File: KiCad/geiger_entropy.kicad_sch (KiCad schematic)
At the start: 34 parts, among them J1 AudioJack2, J2 Jack-DC, J3 ICSP, J4 Conn_01x04_Socket, J5 Conn_01x10_Pin, J6 Conn_01x10_Pin, SW1 RESET, SW2 REV, SW3 FWD, U1 LM393, U2 L7805, U4 ATmega328-P, Y1 16MHz

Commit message: Add BOM and fix signal line debounce issue with a 100pF capacitor - optimise PCB layout
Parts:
- added C11: 100pF, Capacitor_THT:C_Disc_D5.0mm_W2.5mm_P5.00mm, symbol Device:C
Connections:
- net D2: now also C11.1
- net GND: now also C11.2
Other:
- moved on the sheet: L1, R7
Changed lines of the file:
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@@
 	)
 	(junction
+		(at 171.45 105.41)
+		(diameter 0)
+		(color 0 0 0 0)
+	)
+	(junction
 		(at 76.2 91.44)
 		(diameter 0)
@@
 	(wire
 		(pts
+			(xy 171.45 110.49) (xy 171.45 105.41)
+		)
+		(stroke
+			(width 0)
+			(type default)
+		)
+	)
+	(wire
+		(pts
 			(xy 236.22 142.24) (xy 247.65 142.24)
 		)
@@
 	(wire
 		(pts
-			(xy 151.13 69.85) (xy 165.1 69.85)
+			(xy 151.13 69.85) (xy 171.45 69.85)
 		)
 		(stroke
@@
 	(wire
 		(pts
+			(xy 171.45 105.41) (xy 177.8 105.41)
+		)
+		(stroke
+			(width 0)
+			(type default)
+		)
+	)
+	(wire
+		(pts
 			(xy 215.9 31.75) (xy 222.25 31.75)
 		)
@@
 	(wire
 		(pts
+			(xy 171.45 125.73) (xy 171.45 118.11)
+		)
+		(stroke
+			(width 0)
+			(type default)
+		)
+	)
+	(wire
+		(pts
 			(xy 68.58 153.67) (xy 74.93 153.67)
 		)
@@
 	(wire
 		(pts
-			(xy 151.13 105.41) (xy 157.48 105.41)
+			(xy 151.13 105.41) (xy 171.45 105.41)
 		)
 		(stroke
@@
 	)
 	(label "Signal"
-		(at 157.48 105.41 0)
+		(at 177.8 105.41 0)
 		(effects
 			(font
@@
 	(symbol
 		(lib_id "Device:LED")
-		(at 165.1 81.28 90)
+		(at 171.45 81.28 90)
 		(unit 1)
 		(body_style 1)
@@
 		(fields_autoplaced yes)
 		(property "Reference" "L1"
-			(at 168.91 81.5974 90)
+			(at 175.26 81.5974 90)
 			(show_name no)
 			(do_not_autoplace no)
@@
 		)
 		(property "Value" "Yellow"
-			(at 168.91 84.1374 90)
+			(at 175.26 84.1374 90)
 			(show_name no)
 			(do_not_autoplace no)
@@
 		)
 		(property "Footprint" "LED_THT:LED_D3.0mm"
-			(at 165.1 81.28 0)
+			(at 171.45 81.28 0)
 			(hide yes)
 			(show_name no)
@@
 		)
 		(property "Datasheet" ""
-			(at 165.1 81.28 0)
+			(at 171.45 81.28 0)
 			(hide yes)
 			(show_name no)
@@
 		)
 		(property "Description" "Light emitting diode"
-			(at 165.1 81.28 0)
+			(at 171.45 81.28 0)
 			(hide yes)
 			(show_name no)
@@
 		)
 		(property "Sim.Pins" "1=K 2=A"
-			(at 165.1 81.28 0)
+			(at 171.45 81.28 0)
 			(hide yes)
 			(show_name no)
@@
 	)
 	(symbol
+		(lib_id "power:GND")
+		(at 171.45 125.73 0)
+		(unit 1)
+		(body_style 1)
+		(exclude_from_sim no)
+		(in_bom yes)
+		(on_board yes)
+		(in_pos_files yes)
+		(dnp no)
+		(fields_autoplaced yes)
+		(property "Reference" "#PWR019"
+			(at 171.45 132.08 0)
+			(hide yes)
+			(show_name no)
+			(do_not_autoplace no)
+			(effects
+				(font
+					(size 1.27 1.27)
+				)
+			)
+		)
+		(property "Value" "GND"
+			(at 171.45 130.81 0)
+			(show_name no)
+			(do_not_autoplace no)
+			(effects
+				(font
+					(size 1.27 1.27)
+				)
+			)
+		)
+		(property "Footprint" ""
+			(at 171.45 125.73 0)
+			(hide yes)
+			(show_name no)
+			(do_not_autoplace no)
+			(effects
+				(font
+					(size 1.27 1.27)
+				)
+			)
+		)
+		(property "Datasheet" ""
+			(at 171.45 125.73 0)
+			(hide yes)
+			(show_name no)
+			(do_not_autoplace no)
+			(effects
+				(font
+					(size 1.27 1.27)
+				)
+			)
+		)
+		(property "Description" "Power symbol creates a global label with name \"GND\" , ground"
+			(at 171.45 125.73 0)
+			(hide yes)
+			(show_name no)
+			(do_not_autoplace no)
+			(effects
+				(font
+					(size 1.27 1.27)
+				)
+			)
+		)
+		(pin "1"
+		)
+		(instances
+			(project "geiger_entropy"
+				(path "/80ae0d79-0652-4509-a7fb-04f6453bcd03"
+					(reference "#PWR019")
+					(unit 1)
+				)
+			)
+		)
+	)
+	(symbol
 		(lib_id "Device:R")
 		(at 246.38 96.52 0)
@@
 	(symbol
 		(lib_id "Device:R")
-		(at 165.1 73.66 0)
+		(at 171.45 73.66 0)
 		(unit 1)
 		(body_style 1)
@@
 		(fields_autoplaced yes)
 		(property "Reference" "R7"
-			(at 167.64 72.3899 0)
+			(at 173.99 72.3899 0)
 			(show_name no)
 			(do_not_autoplace no)
@@
 		)
 		(property "Value" "1k"
-			(at 167.64 74.9299 0)
+			(at 173.99 74.9299 0)
 			(show_name no)
 			(do_not_autoplace no)
@@
 		)
 		(property "Footprint" "Resistor_THT:R_Axial_DIN0207_L6.3mm_D2.5mm_P10.16mm_Horizontal"
-			(at 163.322 73.66 90)
+			(at 169.672 73.66 90)
 			(hide yes)
 			(show_name no)
@@
 		)
 		(property "Datasheet" ""
-			(at 165.1 73.66 0)
+			(at 171.45 73.66 0)
 			(hide yes)
 			(show_name no)
@@
 		)
 		(property "Description" "Resistor"
-			(at 165.1 73.66 0)
+			(at 171.45 73.66 0)
 			(hide yes)
 			(show_name no)
@@
 	(symbol
 		(lib_id "power:GND")
-		(at 165.1 85.09 0)
+		(at 171.45 85.09 0)
 		(unit 1)
 		(body_style 1)
@@
 		(fields_autoplaced yes)
 		(property "Reference" "#PWR014"
-			(at 165.1 91.44 0)
+			(at 171.45 91.44 0)
 			(hide yes)
 			(show_name no)
@@
 		)
 		(property "Value" "GND"
-			(at 165.1 90.17 0)
+			(at 171.45 90.17 0)
 			(show_name no)
 			(do_not_autoplace no)
@@
 		)
 		(property "Footprint" ""
-			(at 165.1 85.09 0)
+			(at 171.45 85.09 0)
 			(hide yes)
 			(show_name no)
@@
 		)
 		(property "Datasheet" ""
-			(at 165.1 85.09 0)
+			(at 171.45 85.09 0)
 			(hide yes)
 			(show_name no)
@@
 		)
 		(property "Description" "Power symbol creates a global label with name \"GND\" , ground"
-			(at 165.1 85.09 0)
+			(at 171.45 85.09 0)
 			(hide yes)
 			(show_name no)
@@
 					(unit 1)
 				)
+			)
+		)
+	)
+	(symbol
+		(lib_id "Device:C")
+		(at 171.45 114.3 0)
+		(unit 1)
+		(body_style 1)
+		(exclude_from_sim no)
+		(in_bom yes)
+		(on_board yes)
+		(in_pos_files yes)
+		(dnp no)
+		(fields_autoplaced yes)
+		(property "Reference" "C11"
+			(at 175.26 113.0299 0)
+			(show_name no)
+			(do_not_autoplace no)
+			(effects
+				(font
+					(size 1.27 1.27)
+				)
+				(justify left)
+			)
+		)
+		(property "Value" "100pF"
+			(at 175.26 115.5699 0)
+			(show_name no)
+			(do_not_autoplace no)
+			(effects
+				(font
+					(size 1.27 1.27)
+				)
+				(justify left)
+			)
+		)
+		(property "Footprint" "Capacitor_THT:C_Disc_D5.0mm_W2.5mm_P5.00mm"
+			(at 172.4152 118.11 0)
+			(hide yes)
+			(show_name no)
+			(do_not_autoplace no)
+			(effects
+				(font
+					(size 1.27 1.27)
+				)
+			)
+		)
+		(property "Datasheet" ""
+			(at 171.45 114.3 0)
+			(hide yes)
+			(show_name no)
+			(do_not_autoplace no)
+			(effects
+				(font
+					(size 1.27 1.27)
+				)
+			)
+		)
+		(property "Description" "Unpolarized capacitor"
+			(at 171.45 114.3 0)
+			(hide yes)
+			(show_name no)
+			(do_not_autoplace no)
+			(effects
+				(font
+					(size 1.27 1.27)
+				)
+			)
+		)
+		(pin "1"
+		)
+		(pin "2"
+		)
+		(instances
+			(project "geiger_entropy"
+				(path "/80ae0d79-0652-4509-a7fb-04f6453bcd03"
+					(reference "C11")
+					(unit 1)
+				)

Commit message: Update PCB and add hardware license
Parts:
- renumbered C5 to C10, C6 to C2, C7 to C3, C11 to C4, C8 to C5, C9 to C6, C2 to C7, C4 to C8, C3 to C9, J4 to J2, J5 to J3, J6 to J4, J2 to J5, J3 to J6, R2 to R1, R3 to R2, R8 to R3, R1 to R4, R4 to R5, R9 to R6, R6 to R8, R5 to R9, SW2 to SW1, SW3 to SW2, SW1 to SW3, U4 to U2, U2 to U3

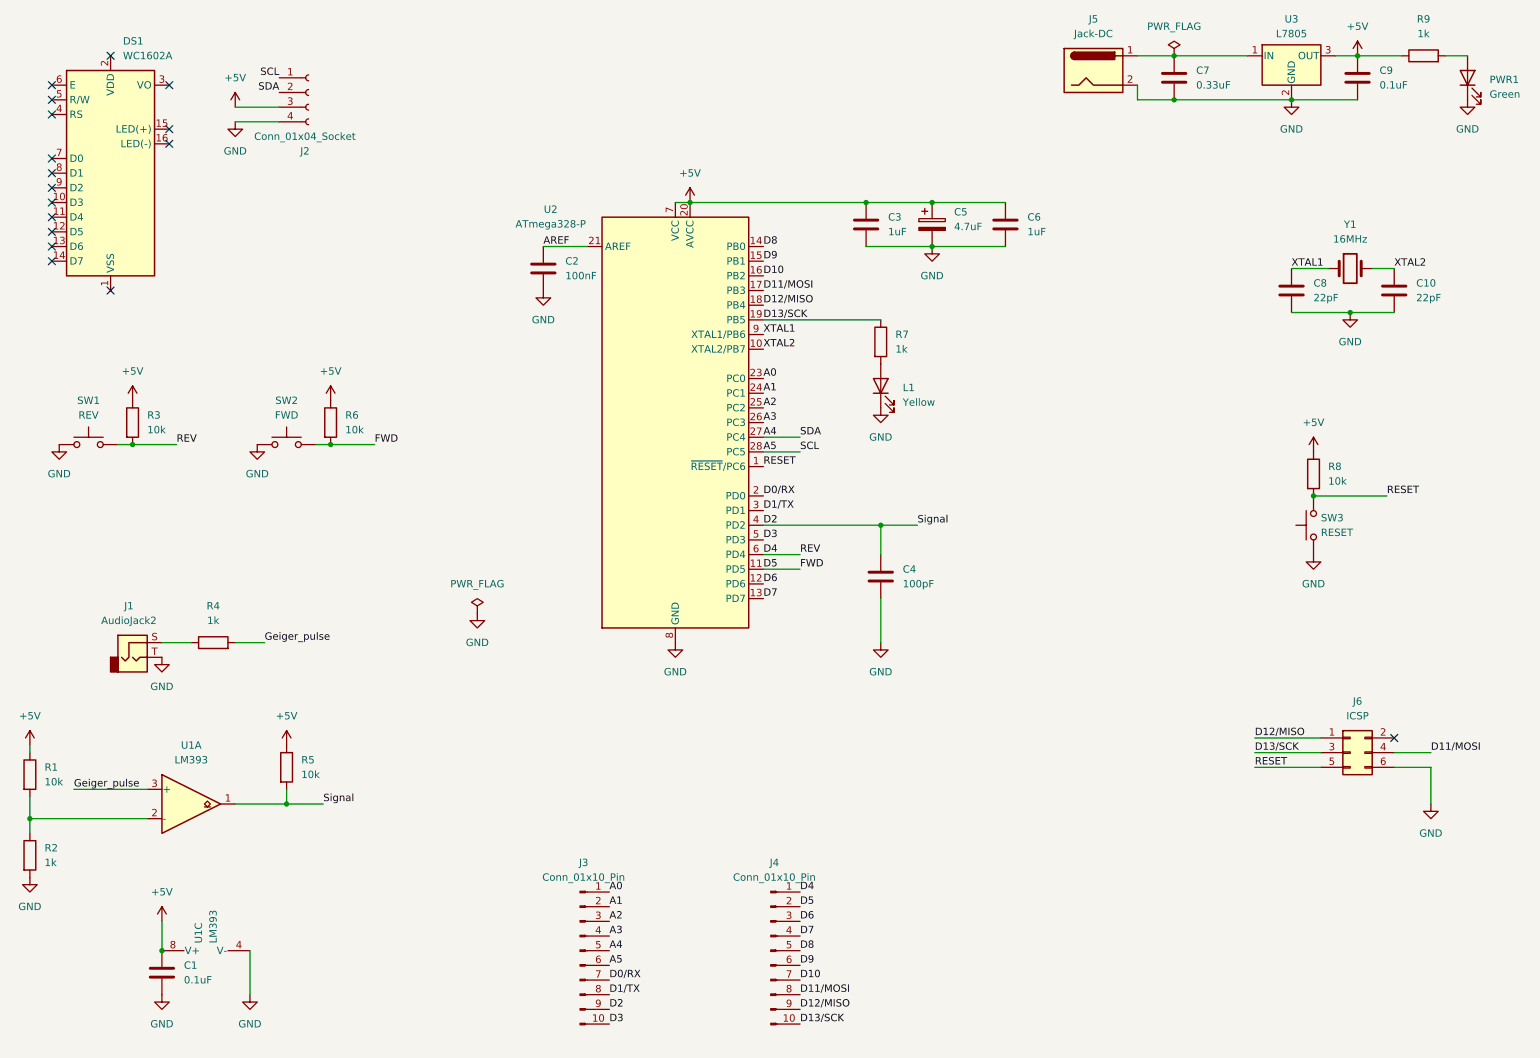
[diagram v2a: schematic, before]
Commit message: Update PCB to add hysterisis to the LM393 comparator
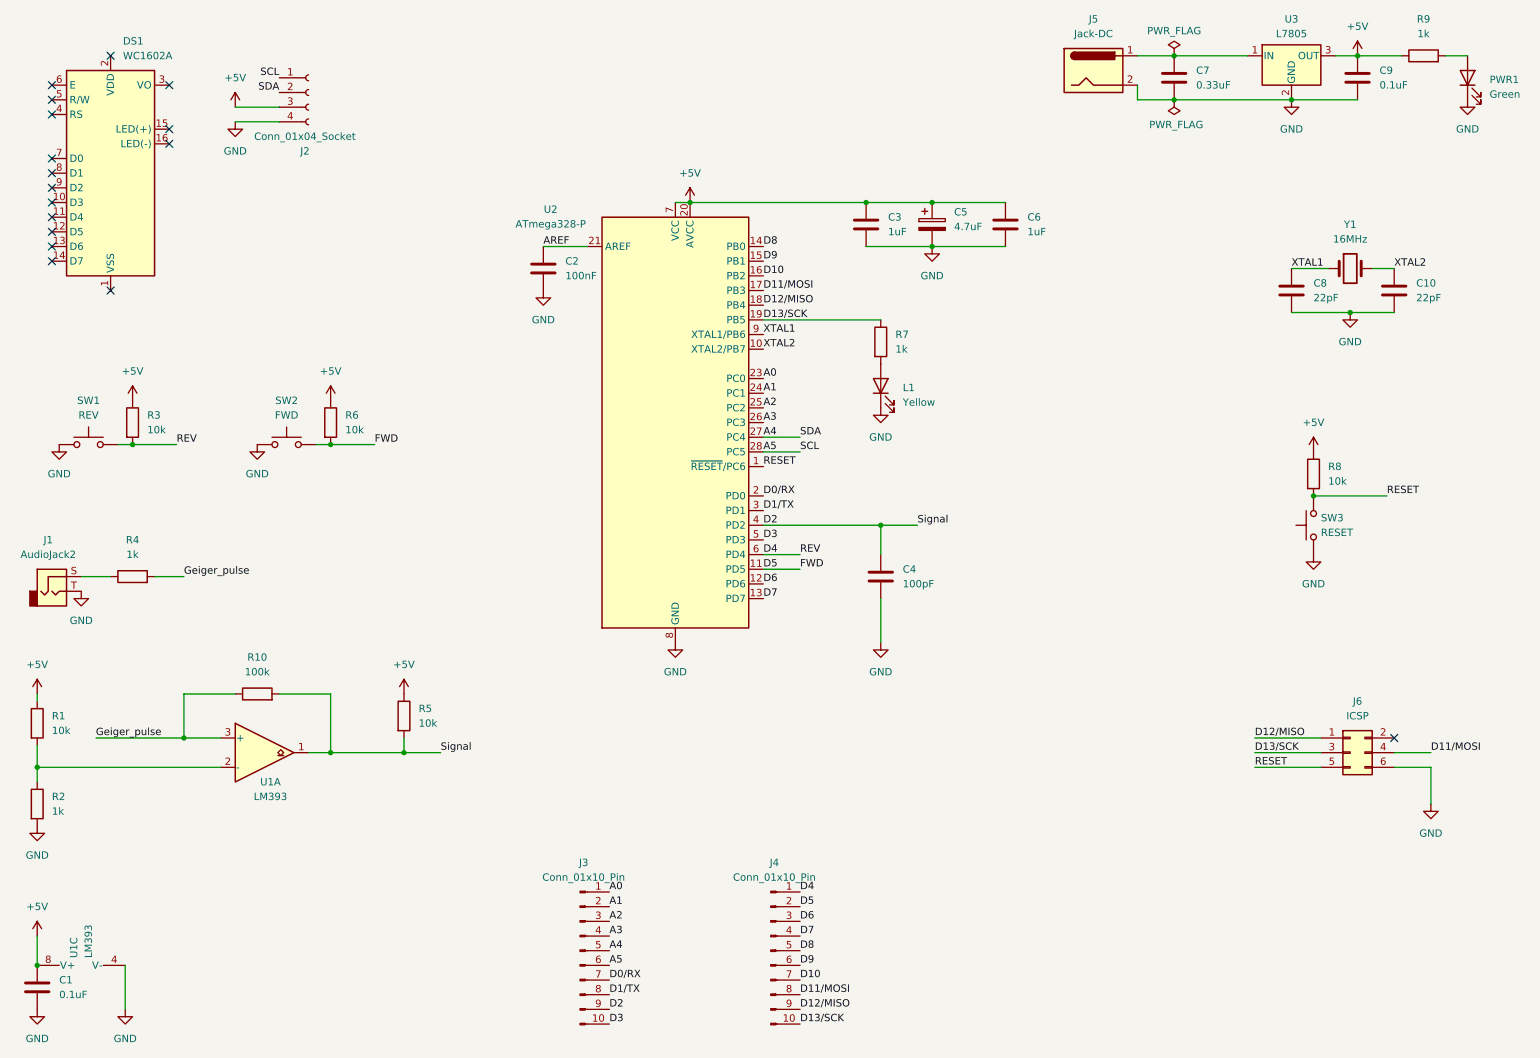
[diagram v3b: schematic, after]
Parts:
- added R10: 100k, Resistor_THT:R_Axial_DIN0207_L6.3mm_D2.5mm_P10.16mm_Horizontal, symbol Device:R
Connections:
- net D2: now also R10.2
- net Geiger_pulse: now also R10.1
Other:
- moved on the sheet: C1, J1, R1, R2, R4, R5, U1A, U1C

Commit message: Modify PCB
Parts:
- removed J3, J4: Conn_01x10_Pin, Connector_PinHeader_2.54mm:PinHeader_1x10_P2.54mm_Vertical, symbol Connector:Conn_01x10_Pin
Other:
- note added: "Entropy32"
